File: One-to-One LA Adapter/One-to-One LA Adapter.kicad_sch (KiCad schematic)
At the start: 1 part, among them J1 Cerberus_Expansion

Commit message: one-to-one ready for pcb
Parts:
- added J2: Card_Header, Connector_PinHeader_2.54mm:PinHeader_2x20_P2.54mm_Vertical, symbol Connector_Generic:Conn_02x20_Odd_Even
- added J3: LA_Header, Connector_PinHeader_2.54mm:PinHeader_2x20_P2.54mm_Vertical, symbol Connector_Generic:Conn_02x20_Odd_Even
- added J4: XE_Header, symbol Connector_Generic:Conn_01x03
- J1: footprint Connector_PinHeader_2.54mm:PinHeader_2x20_P2.54mm_Vertical -> Connector_PinSocket_2.54mm:PinSocket_2x20_P2.54mm_Vertical
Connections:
- net GND: now also J2.2 (Pin_2), J2.36 (Pin_36), J2.38 (Pin_38), J2.40 (Pin_40), J3.2 (Pin_2), J3.36 (Pin_36), J3.38 (Pin_38), J3.40 (Pin_40), J4.3 (Pin_3)
- net XA0: now also J2.11 (Pin_11), J3.11 (Pin_11)
- net XA1: now also J2.12 (Pin_12), J3.12 (Pin_12)
- net XA10: now also J2.21 (Pin_21), J3.21 (Pin_21)
- net XA11: now also J2.22 (Pin_22), J3.22 (Pin_22)
- net XA12: now also J2.23 (Pin_23), J3.23 (Pin_23)
- net XA13: now also J2.24 (Pin_24), J3.24 (Pin_24)
- net XA14: now also J2.25 (Pin_25), J3.25 (Pin_25)
- net XA15: now also J2.26 (Pin_26), J3.26 (Pin_26)
- net XA2: now also J2.13 (Pin_13), J3.13 (Pin_13)
- net XA3: now also J2.14 (Pin_14), J3.14 (Pin_14)
- net XA4: now also J2.15 (Pin_15), J3.15 (Pin_15)
- net XA5: now also J2.16 (Pin_16), J3.16 (Pin_16)
- net XA6: now also J2.17 (Pin_17), J3.17 (Pin_17)
- net XA7: now also J2.18 (Pin_18), J3.18 (Pin_18)
- net XA8: now also J2.19 (Pin_19), J3.19 (Pin_19)
- net XA9: now also J2.20 (Pin_20), J3.20 (Pin_20)
- net XBUSACK: now also J2.7 (Pin_7), J3.7 (Pin_7)
- net XBUSREQ: now also J2.5 (Pin_5), J3.5 (Pin_5)
- net XCLK: now also J2.1 (Pin_1), J3.1 (Pin_1)
- net XD0: now also J2.27 (Pin_27), J3.27 (Pin_27)
- net XD1: now also J2.28 (Pin_28), J3.28 (Pin_28)
- net XD2: now also J2.29 (Pin_29), J3.29 (Pin_29)
- net XD3: now also J2.30 (Pin_30), J3.30 (Pin_30)
- net XD4: now also J2.31 (Pin_31), J3.31 (Pin_31)
- net XD5: now also J2.32 (Pin_32), J3.32 (Pin_32)
- net XD6: now also J2.33 (Pin_33), J3.33 (Pin_33)
- net XD7: now also J2.34 (Pin_34), J3.34 (Pin_34)
- net XE: now also J2.4 (Pin_4), J3.4 (Pin_4), J4.2 (Pin_2)
- net XIN: now also J2.39 (Pin_39), J3.39 (Pin_39)
- net XIRQ: now also J2.8 (Pin_8), J3.8 (Pin_8)
- net XRD: now also J2.9 (Pin_9), J3.9 (Pin_9)
- net XSLC: now also J2.6 (Pin_6), J3.6 (Pin_6)
- net XWR: now also J2.10 (Pin_10), J3.10 (Pin_10)
- net 5V renamed +5V
- net +5V: now also J2.3 (Pin_3), J2.35 (Pin_35), J2.37 (Pin_37), J3.3 (Pin_3), J3.35 (Pin_35), J3.37 (Pin_37), J4.1 (Pin_1)
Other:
- moved on the sheet: J1

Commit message: unrouted 0
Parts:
- added D1: Pwr, LED_SMD:LED_1206_3216Metric_Pad1.42x1.75mm_HandSolder, symbol Device:LED_Small
- added R1: 1k, Resistor_SMD:R_0805_2012Metric_Pad1.20x1.40mm_HandSolder, symbol My Library:R_0805
- J4: footprint (none) -> Connector_PinHeader_2.54mm:PinHeader_1x03_P2.54mm_Vertical
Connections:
- net +5V: now also R1.1
- net GND: now also D1.1 (K)
- new net: D1.2 (A), R1.2
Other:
- moved on the sheet: J4

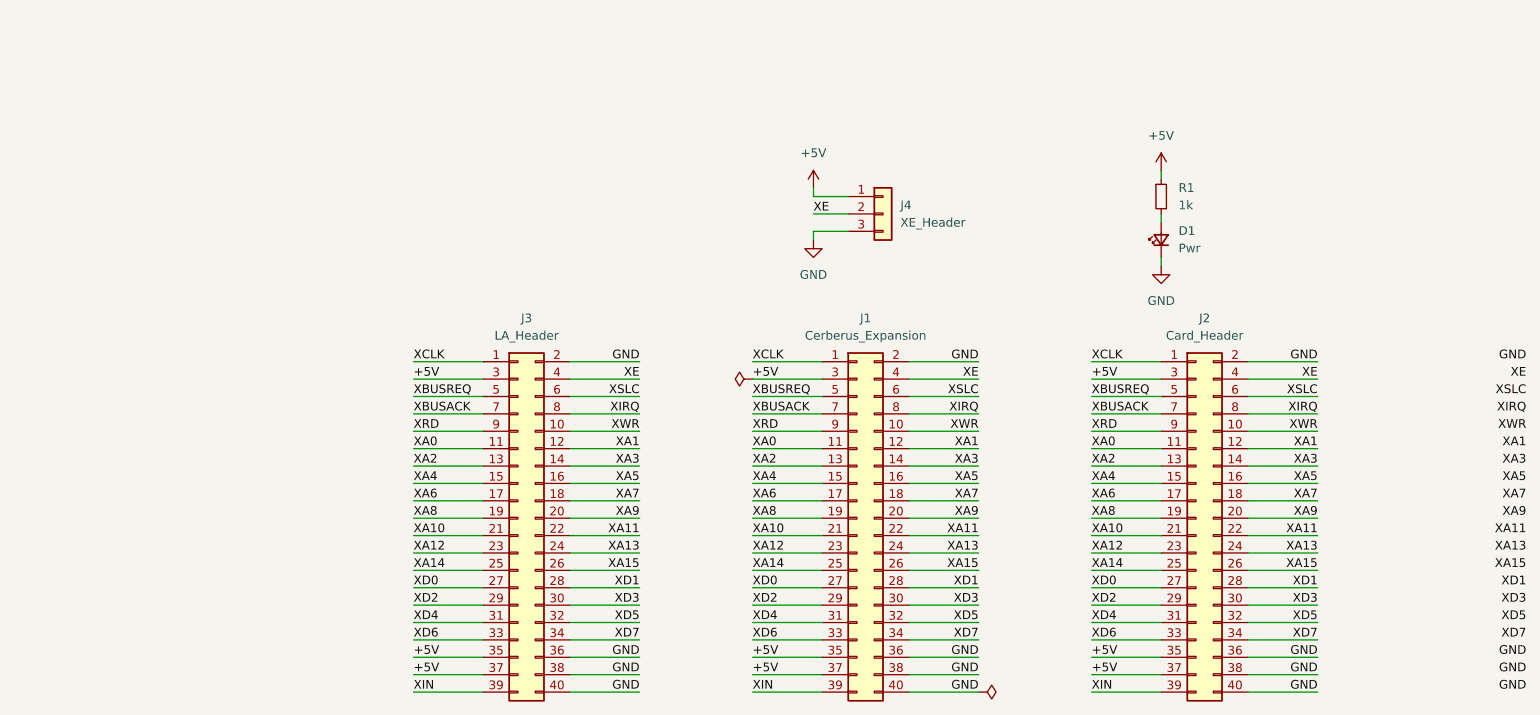
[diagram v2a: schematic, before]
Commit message: Documentation updates. (No design changes made.)
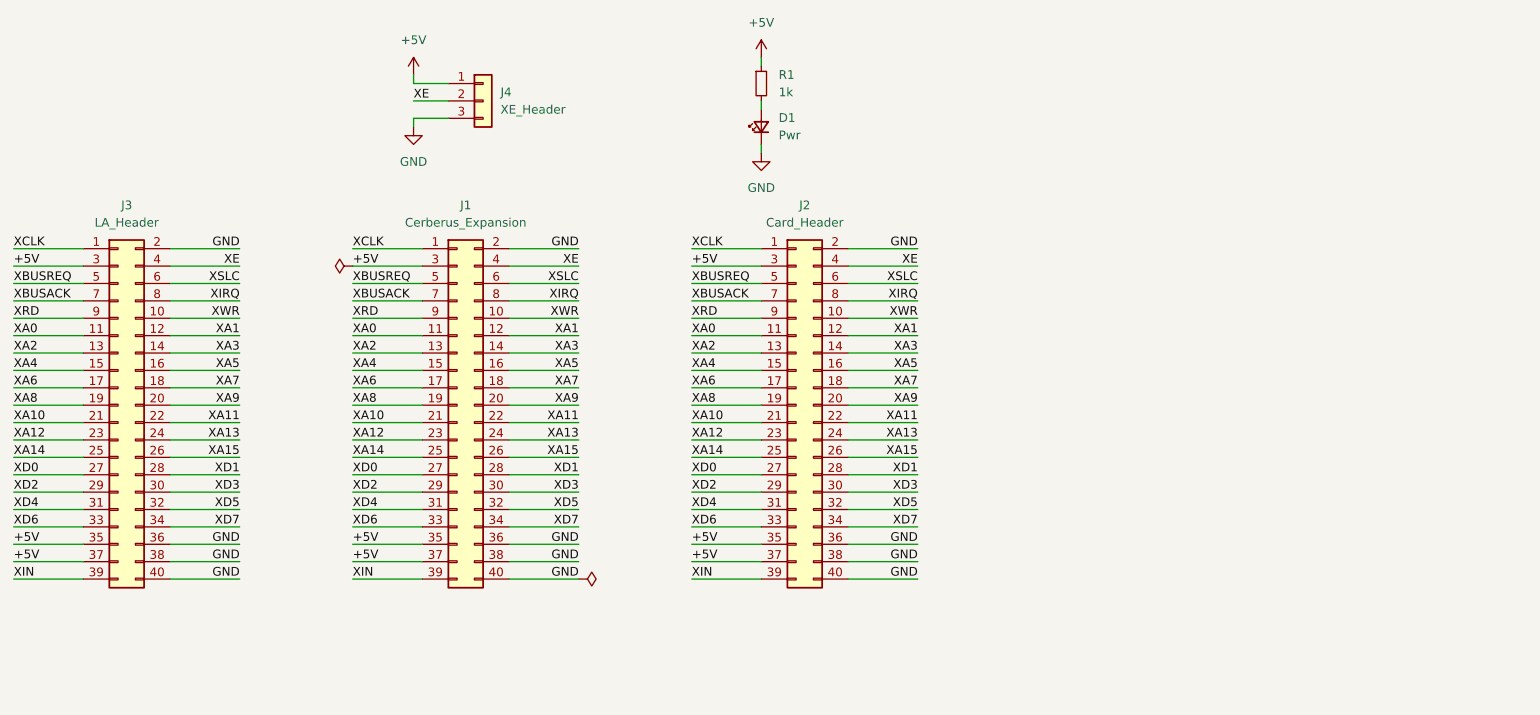
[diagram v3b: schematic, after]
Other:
- company: (none) -> @baldengineer
- title: (none) -> CERBERUS 2100(tm) Logic Analyzer Adapter (1 to 1 map)
- moved on the sheet: D1, J1, J2, J3, J4, R1
